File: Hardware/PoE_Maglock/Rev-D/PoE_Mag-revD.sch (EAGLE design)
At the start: 89 parts, among them IC2 ATMEGA32U4-MU, J2 1X2-3.5MM, J3 1X2-3.5MM, J4 1X2-3.5MM, J5 1X2-3.5MM, J6 10103594-0001LF, Q1 35A/25V/8.5mΩ, Q3 35A/25V/8.5mΩ, Q5 35A/25V/8.5mΩ, Q6 35A/25V/8.5mΩ, SW1 SPST_TACT-KMR2, T1 DMG3415U, U2 SPX3819-3.3, U3 LMV358IDGKR, U4 W5500, X2 J1011FHANRUN, Y4 8MHz

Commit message: HEEP-654 passive poe maglock for review
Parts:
- removed C2: 100uF 25V, microbuilder:CAP_ELECTROLYTICPANASONIC_D
- removed C5: 470uF 25V, SparkFun-Passives:CAP_POLG
- removed C6, C8: 10µF, microbuilder:CAP_CERAMIC0603MINI
- removed C7: 1uF, microbuilder:CAP_CERAMIC0603MINI
- removed R13, R14: 10K, microbuilder:RESISTOR_0603_NOOUT
- removed T1: DMG3415U, zetex:PMOSSOT23
- removed U$1: SILVERTEL_POEMICRO, Heep:SILVERTEL_POEMICRO
- removed U$16: AG5200AG5300, Heep:AG5200AG5300
- removed U2: SPX3819-3.3, microbuilder:VREG_SOT23-5
- removed U3: LMV358IDGKR, linear:LMV358MMX
- added D10, D11, D8, D9: (no value), microbuilder:DIODESOD-123
- added D6, D7: PMEG4030ER, microbuilder:DIODESOD-123
- C1: value 10uF -> (none); device microbuilder:CAP_CERAMIC_0805MP -> microbuilder:CAP_ELECTROLYTICPANASONIC_D
- X2: value J1011FHANRUN -> J1011FTOP_TAB; device Heep:J1011FHANRUN -> Heep:J1011FTOP_TAB
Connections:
- removed net +5V: C12.1, C13.1, C6.1, J7.2, L1.2, T1.S, U$19.FB, U2.EN, U2.IN, U3P.V+
- removed net CMP: R13.1, R14.2, U3A.+IN
- removed net GATE_CMD: T1.G, U3A.OUT
- removed net N$1: U$1.VIN-, U$16.VIN-, X2.POE-
- removed net N$15: C14.2, L1.1, U$19.VSW
- removed net N$2: U$1.VIN+, U$16.VIN+, X2.POE+
- new net N$16: C14.2, D6.C, L1.1, U$19.VSW
- net +3V3: now also C12.1, C13.1, L1.2, U$19.FB; no longer C7.1, C8.1, U2.OUT, U3A.-IN
- net DRAIN1: now also D11.A
- net DRAIN2: now also D8.A
- net DRAIN3: now also D9.A
- net DRAIN4: now also D10.A
- net GND: now also C1.-, D6.A, X2.POE-; no longer C1.1, C2.-, C5.-, C6.2, C7.2, C8.2, R14.1, U$1.-VDC, U$16.-VDC, U2.GND, U3P.V-
- net VBAT: now also C1.+, D10.C, D11.C, D7.C, D8.C, D9.C, X2.POE+; no longer C1.2, C2.+, C5.+, R13.2, U$1.+VDC, U$16.+VDC
- net VBUS: now also D7.A, J7.2; no longer T1.D
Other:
- note added: "POWER SUPPLY: 3.3V BUCK"
- note removed: "POWER AND FILTERING"
- note removed: "POWER SUPPLY SELECTION"
- note removed: "POWER SUPPLY: 5V"
- note removed: "VBAT = PoE V+"
- note removed: "VOLTAGE SELECT (3.3V DEFAULT)"
- moved on the sheet: C12, C13, C14, C4, J11, J12, L1

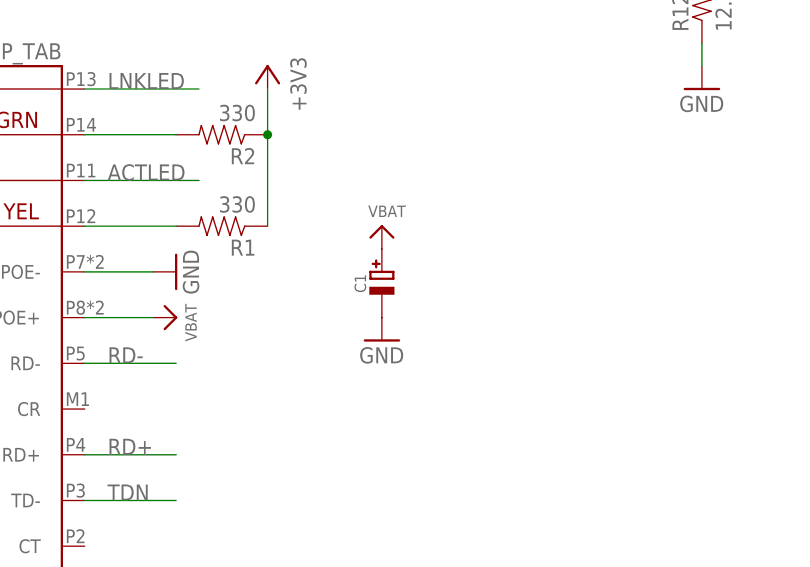
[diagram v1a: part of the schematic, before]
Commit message: HEEP-688 updated value
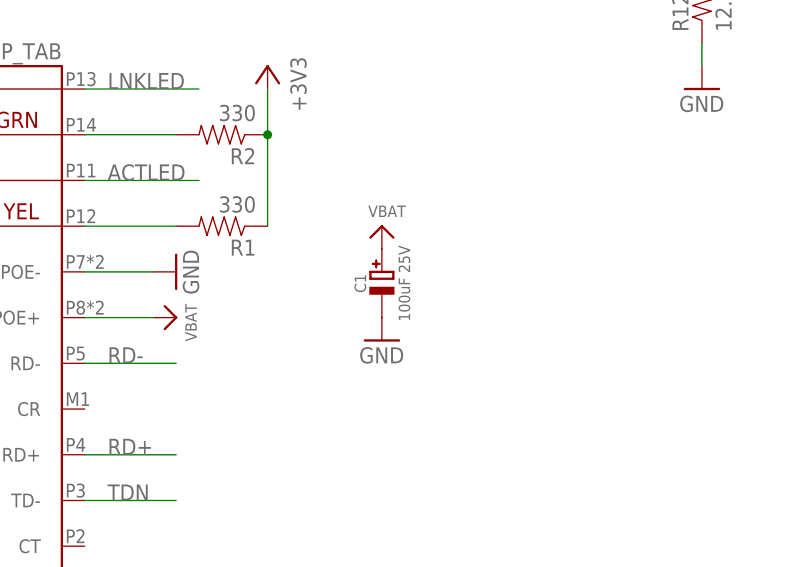
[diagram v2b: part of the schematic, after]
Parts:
- C1: value (none) -> 100uF 25V
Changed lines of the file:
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@@
 <part name="U$1" library="microbuilder" deviceset="VBAT" device=""/>
 <part name="GND18" library="SparkFun-Aesthetics" deviceset="GND" device=""/>
-<part name="C1" library="microbuilder" deviceset="CAP_ELECTROLYTIC" device="PANASONIC_D"/>
+<part name="C1" library="microbuilder" deviceset="CAP_ELECTROLYTIC" device="PANASONIC_D" value="100uF 25V"/>
 <part name="U$2" library="microbuilder" deviceset="VBAT" device=""/>
 <part name="GND24" library="SparkFun-Aesthetics" deviceset="GND" device=""/>
